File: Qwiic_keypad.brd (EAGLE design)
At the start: 31.8 x 25.4 mm, 25 parts, among them J2 SMD, J3 PTH, J4 SMD, J6 AVR_SPI_PROG_3X2TESTPOINTS, U3 ATTINY84

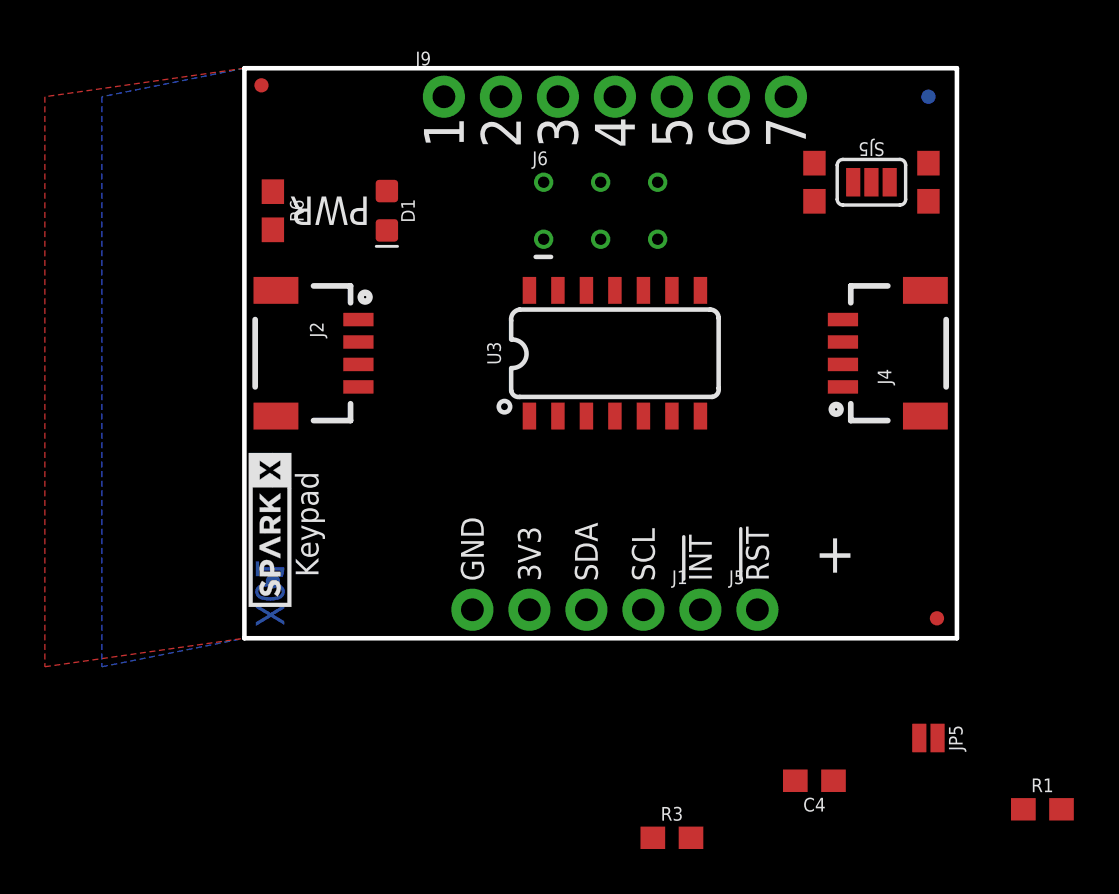
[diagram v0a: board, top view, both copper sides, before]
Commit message: starting new route
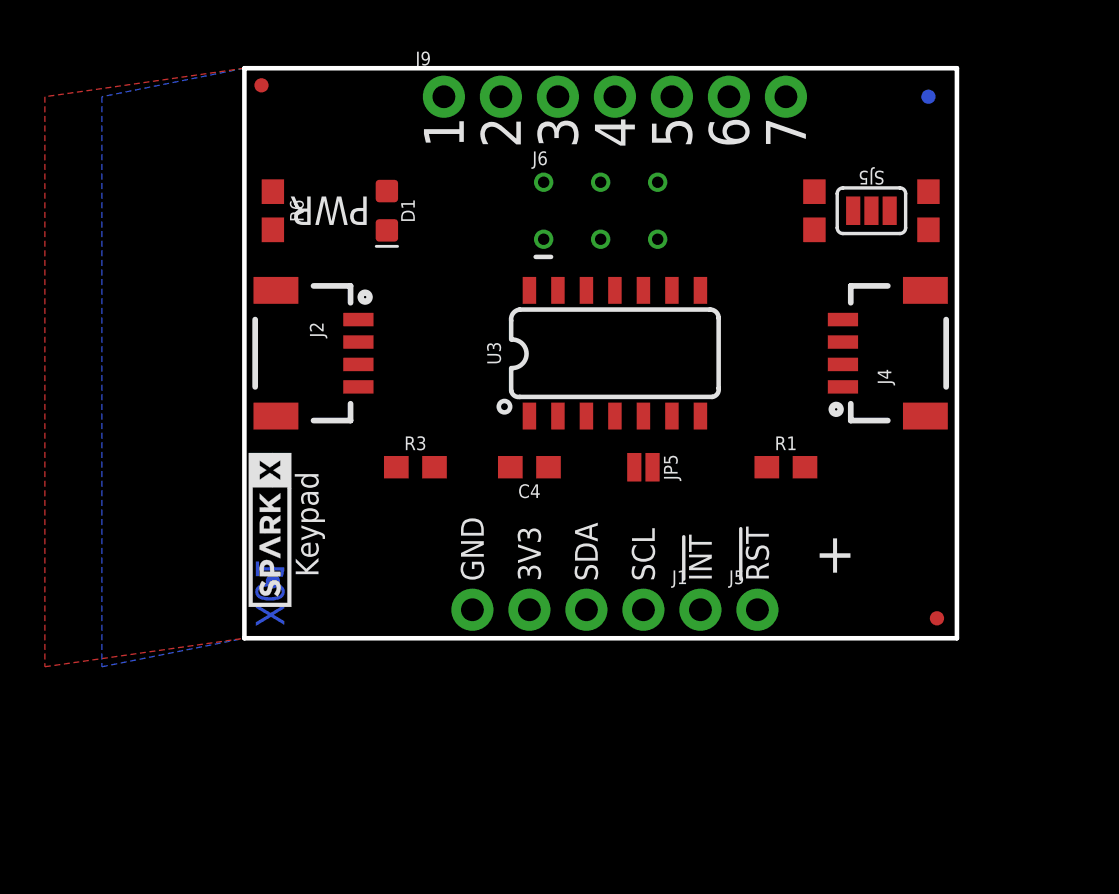
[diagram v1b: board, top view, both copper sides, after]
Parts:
- moved R3 20.1 mm to (7.62, 7.62)
- moved R1 19.1 mm to (24.1, 7.62)
- moved C4 18.9 mm to (12.7, 7.62)
- moved JP5 17.5 mm to (17.8, 7.62)
- moved R2 1.27 mm to (25.4, 19.1)
- moved R4 1.27 mm to (30.5, 19.1), turned to 90 degrees
- moved SJ5 1.27 mm to (27.9, 19.1)
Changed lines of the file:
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@@
 <element name="FRAME1" library="SparkFun-Aesthetics" package="CREATIVE_COMMONS" value="FRAME-LETTER" x="-16.51" y="-49.53"/>
 <element name="U$2" library="SparkX" package="SPARKX-SMALL" value="SPARKX-LOGO3" x="1.143" y="4.826" rot="R90"/>
-<element name="C4" library="SparkFun-Capacitors" package="0603" value="0.1uF" x="25.4" y="-6.35" rot="R180">
-<attribute name="PROD_ID" value="CAP-00810" x="25.4" y="-6.35" size="1.778" layer="27" font="vector" ratio="15" rot="R180" display="off"/>
+<element name="C4" library="SparkFun-Capacitors" package="0603" value="0.1uF" x="12.7" y="7.62" rot="R180">
+<attribute name="PROD_ID" value="CAP-00810" x="12.7" y="7.62" size="1.778" layer="27" font="vector" ratio="15" rot="R180" display="off"/>
 </element>
 <element name="J4" library="SparkX" package="1X04_1MM_RA" value="SMD" x="26.67" y="12.7" rot="R90"/>
 <element name="LOGO1" library="SparkFun-Aesthetics" package="OSHW-LOGO-MINI" value="OSHW-LOGOMINI" x="2.54" y="21.59" rot="MR0"/>
 <element name="U$1" library="SparkX" package="SPARKX-SMALL" value="SPARKX-LOGO3" x="30.48" y="12.7" rot="MR90"/>
-<element name="R2" library="SparkFun-Resistors" package="0603" value="2.2k" x="25.4" y="20.32" smashed="yes" rot="R90">
-<attribute name="PROD_ID" value="RES-08272" x="21.59" y="20.32" size="1.778" layer="27" font="vector" ratio="15" rot="R90" display="off"/>
-<attribute name="VALUE" x="26.162" y="20.32" size="0.6096" layer="27" font="vector" ratio="20" rot="R90" align="top-center"/>
+<element name="R2" library="SparkFun-Resistors" package="0603" value="2.2k" x="25.4" y="19.05" smashed="yes" rot="R90">
+<attribute name="PROD_ID" value="RES-08272" x="21.59" y="19.05" size="1.778" layer="27" font="vector" ratio="15" rot="R90" display="off"/>
+<attribute name="VALUE" x="26.162" y="19.05" size="0.6096" layer="27" font="vector" ratio="20" rot="R90" align="top-center"/>
 </element>
-<element name="R4" library="SparkFun-Resistors" package="0603" value="2.2k" x="30.48" y="20.32" smashed="yes" rot="R270">
-<attribute name="PROD_ID" value="RES-08272" x="34.29" y="20.32" size="1.778" layer="27" font="vector" ratio="15" rot="R270" display="off"/>
-<attribute name="VALUE" x="29.718" y="20.32" size="0.6096" layer="27" font="vector" ratio="20" rot="R270" align="top-center"/>
+<element name="R4" library="SparkFun-Resistors" package="0603" value="2.2k" x="30.48" y="19.05" smashed="yes" rot="R90">
+<attribute name="PROD_ID" value="RES-08272" x="26.67" y="19.05" size="1.778" layer="27" font="vector" ratio="15" rot="R90" display="off"/>
+<attribute name="VALUE" x="31.242" y="19.05" size="0.6096" layer="27" font="vector" ratio="20" rot="R90" align="top-center"/>
 </element>
-<element name="SJ5" library="SparkFun-Jumpers" package="SMT-JUMPER_3_2-NC_PASTE_SILK" value="" x="27.94" y="20.32" smashed="yes">
-<attribute name="NAME" x="27.94" y="22.098" size="0.6096" layer="21" font="vector" ratio="20" rot="SR180" align="bottom-center"/>
-<attribute name="VALUE" x="27.94" y="19.177" size="0.6096" layer="27" font="vector" ratio="20" align="top-center"/>
+<element name="SJ5" library="SparkFun-Jumpers" package="SMT-JUMPER_3_2-NC_PASTE_SILK" value="" x="27.94" y="19.05" smashed="yes">
+<attribute name="NAME" x="27.94" y="20.828" size="0.6096" layer="21" font="vector" ratio="20" rot="SR180" align="bottom-center"/>
+<attribute name="VALUE" x="27.94" y="17.907" size="0.6096" layer="27" font="vector" ratio="20" align="top-center"/>
 </element>
 <element name="J1" library="SparkFun-Connectors" package="1X01_NO_SILK" value="" x="20.32" y="1.27"/>
-<element name="R3" library="SparkFun-Resistors" package="0603" value="10k" x="19.05" y="-8.89">
-<attribute name="PROD_ID" value="RES-08272" x="19.05" y="-8.89" size="1.778" layer="27" font="vector" ratio="15" display="off"/>
+<element name="R3" library="SparkFun-Resistors" package="0603" value="10k" x="7.62" y="7.62">
+<attribute name="PROD_ID" value="RES-08272" x="7.62" y="7.62" size="1.778" layer="27" font="vector" ratio="15" display="off"/>
 </element>
-<element name="JP5" library="SparkFun-Jumpers" package="SMT-JUMPER_2_NC_PASTE_NO-SILK" value="JUMPER-SMT_2_NC_PASTE_NO-SILK" x="30.48" y="-4.445" smashed="yes">
-<attribute name="NAME" x="32.004" y="-4.445" size="0.6096" layer="21" font="vector" ratio="20" rot="SR90" align="bottom-center"/>
-<attribute name="VALUE" x="30.48" y="-5.588" size="0.6096" layer="27" font="vector" ratio="20" align="top-center"/>
+<element name="JP5" library="SparkFun-Jumpers" package="SMT-JUMPER_2_NC_PASTE_NO-SILK" value="JUMPER-SMT_2_NC_PASTE_NO-SILK" x="17.78" y="7.62" smashed="yes">
+<attribute name="NAME" x="19.304" y="7.62" size="0.6096" layer="21" font="vector" ratio="20" rot="SR90" align="bottom-center"/>
+<attribute name="VALUE" x="17.78" y="6.477" size="0.6096" layer="27" font="vector" ratio="20" align="top-center"/>
 </element>
 <element name="U3" library="SparkFun-IC-Microcontroller" package="SO14" value="ATTINY84" x="15.875" y="12.7">
@@
 <attribute name="PROD_ID" value="IC-11285" x="15.875" y="12.7" size="1.778" layer="27" display="off"/>
 </element>
-<element name="R1" library="SparkFun-Resistors" package="0603" value="4.7k" x="35.56" y="-7.62">
-<attribute name="PROD_ID" value="RES-08272" x="35.56" y="-7.62" size="1.778" layer="27" font="vector" ratio="15" display="off"/>
+<element name="R1" library="SparkFun-Resistors" package="0603" value="4.7k" x="24.13" y="7.62">
+<attribute name="PROD_ID" value="RES-08272" x="24.13" y="7.62" size="1.778" layer="27" font="vector" ratio="15" display="off"/>
 </element>
 <element name="J6" library="SparkFun-Connectors" package="2X3_TEST_POINTS" value="AVR_SPI_PROG_3X2TESTPOINTS" x="15.875" y="19.05"/>
@@
 <contactref element="J6" pad="2"/>
 <contactref element="R6" pad="2"/>
-<wire x1="26.67" y1="12.2" x2="27.94" y2="20.32" width="0" layer="19" extent="1-1"/>
+<wire x1="26.67" y1="12.2" x2="27.94" y2="19.05" width="0" layer="19" extent="1-1"/>
 <wire x1="12.7" y1="9.9" x2="26.67" y2="12.2" width="0" layer="19" extent="1-1"/>
 <wire x1="5.08" y1="13.2" x2="12.7" y2="9.9" width="0" layer="19" extent="1-1"/>
@@
 <wire x1="12.7" y1="1.27" x2="12.7" y2="9.9" width="0" layer="19" extent="1-1"/>
 <wire x1="13.335" y1="20.32" x2="5.08" y2="13.2" width="0" layer="19" extent="1-1"/>
-<wire x1="26.25" y1="-6.35" x2="12.7" y2="1.27" width="0" layer="19" extent="1-1"/>
-<wire x1="30.8864" y1="-4.445" x2="26.25" y2="-6.35" width="0" layer="19" extent="1-1"/>
-<wire x1="36.41" y1="-7.62" x2="30.8864" y2="-4.445" width="0" layer="19" extent="1-1"/>
+<wire x1="13.55" y1="7.62" x2="12.7" y2="1.27" width="0" layer="19" extent="1-1"/>
+<wire x1="18.1864" y1="7.62" x2="13.55" y2="7.62" width="0" layer="19" extent="1-1"/>
+<wire x1="24.98" y1="7.62" x2="18.1864" y2="7.62" width="0" layer="19" extent="1-1"/>
 </signal>
 <signal name="GND">
@@
 <wire x1="26.67" y1="11.2" x2="18.415" y2="20.32" width="0" layer="19" extent="1-1"/>
 <wire x1="10.16" y1="1.27" x2="5.08" y2="14.2" width="0" layer="19" extent="1-1"/>
-<wire x1="18.2" y1="-8.89" x2="10.16" y2="1.27" width="0" layer="19" extent="1-1"/>
-<wire x1="24.55" y1="-6.35" x2="18.2" y2="-8.89" width="0" layer="19" extent="1-1"/>
+<wire x1="6.77" y1="7.62" x2="10.16" y2="1.27" width="0" layer="19" extent="1-1"/>
+<wire x1="11.85" y1="7.62" x2="6.77" y2="7.62" width="0" layer="19" extent="1-1"/>
 </signal>
 <signal name="SCL_PU1">
 <contactref element="SJ5" pad="1"/>
 <contactref element="R2" pad="2"/>
-<wire x1="25.4" y1="21.17" x2="27.1272" y2="20.32" width="0" layer="19" extent="1-1"/>
+<wire x1="25.4" y1="19.9" x2="27.1272" y2="19.05" width="0" layer="19" extent="1-1"/>
 </signal>
 <signal name="SDA_PU1">
 <contactref element="SJ5" pad="3"/>
 <contactref element="R4" pad="2"/>
-<wire x1="28.7528" y1="20.32" x2="30.48" y2="19.47" width="0" layer="19" extent="1-1"/>
+<wire x1="28.7528" y1="19.05" x2="30.48" y2="19.9" width="0" layer="19" extent="1-1"/>
 </signal>
 <signal name="!INT">
@@
 <contactref element="JP5" pad="1"/>
 <contactref element="U3" pad="3"/>
-<wire x1="19.9" y1="-8.89" x2="30.0736" y2="-4.445" width="0" layer="19" extent="1-1"/>
-<wire x1="15.24" y1="9.9" x2="19.9" y2="-8.89" width="0" layer="19" extent="1-1"/>
+<wire x1="8.47" y1="7.62" x2="17.3736" y2="7.62" width="0" layer="19" extent="1-1"/>
+<wire x1="15.24" y1="9.9" x2="8.47" y2="7.62" width="0" layer="19" extent="1-1"/>
 </signal>
 <signal name="4">
@@
 <wire x1="16.51" y1="9.9" x2="18.415" y2="17.78" width="0" layer="19" extent="1-1"/>
 <wire x1="22.86" y1="1.27" x2="16.51" y2="9.9" width="0" layer="19" extent="1-1"/>
-<wire x1="34.71" y1="-7.62" x2="22.86" y2="1.27" width="0" layer="19" extent="1-1"/>
+<wire x1="23.28" y1="7.62" x2="22.86" y2="1.27" width="0" layer="19" extent="1-1"/>
 </signal>
 <signal name="N$1">
@@
 <contactref element="J2" pad="4"/>
 <contactref element="J4" pad="4"/>
-<wire x1="26.67" y1="14.2" x2="25.4" y2="19.47" width="0" layer="19" extent="1-1"/>
+<wire x1="26.67" y1="14.2" x2="25.4" y2="18.2" width="0" layer="19" extent="1-1"/>
 <wire x1="19.05" y1="15.5" x2="26.67" y2="14.2" width="0" layer="19" extent="1-1"/>
 <wire x1="15.875" y1="17.78" x2="19.05" y2="15.5" width="0" layer="19" extent="1-1"/>
@@
 <contactref element="J2" pad="3"/>
 <contactref element="J4" pad="3"/>
-<wire x1="26.67" y1="13.2" x2="30.48" y2="21.17" width="0" layer="19" extent="1-1"/>
+<wire x1="26.67" y1="13.2" x2="30.48" y2="18.2" width="0" layer="19" extent="1-1"/>
 <wire x1="20.32" y1="9.9" x2="26.67" y2="13.2" width="0" layer="19" extent="1-1"/>
 <wire x1="15.24" y1="1.27" x2="20.32" y2="9.9" width="0" layer="19" extent="1-1"/>
